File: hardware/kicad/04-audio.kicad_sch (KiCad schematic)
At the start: 9 parts, among them U5 PAM8403

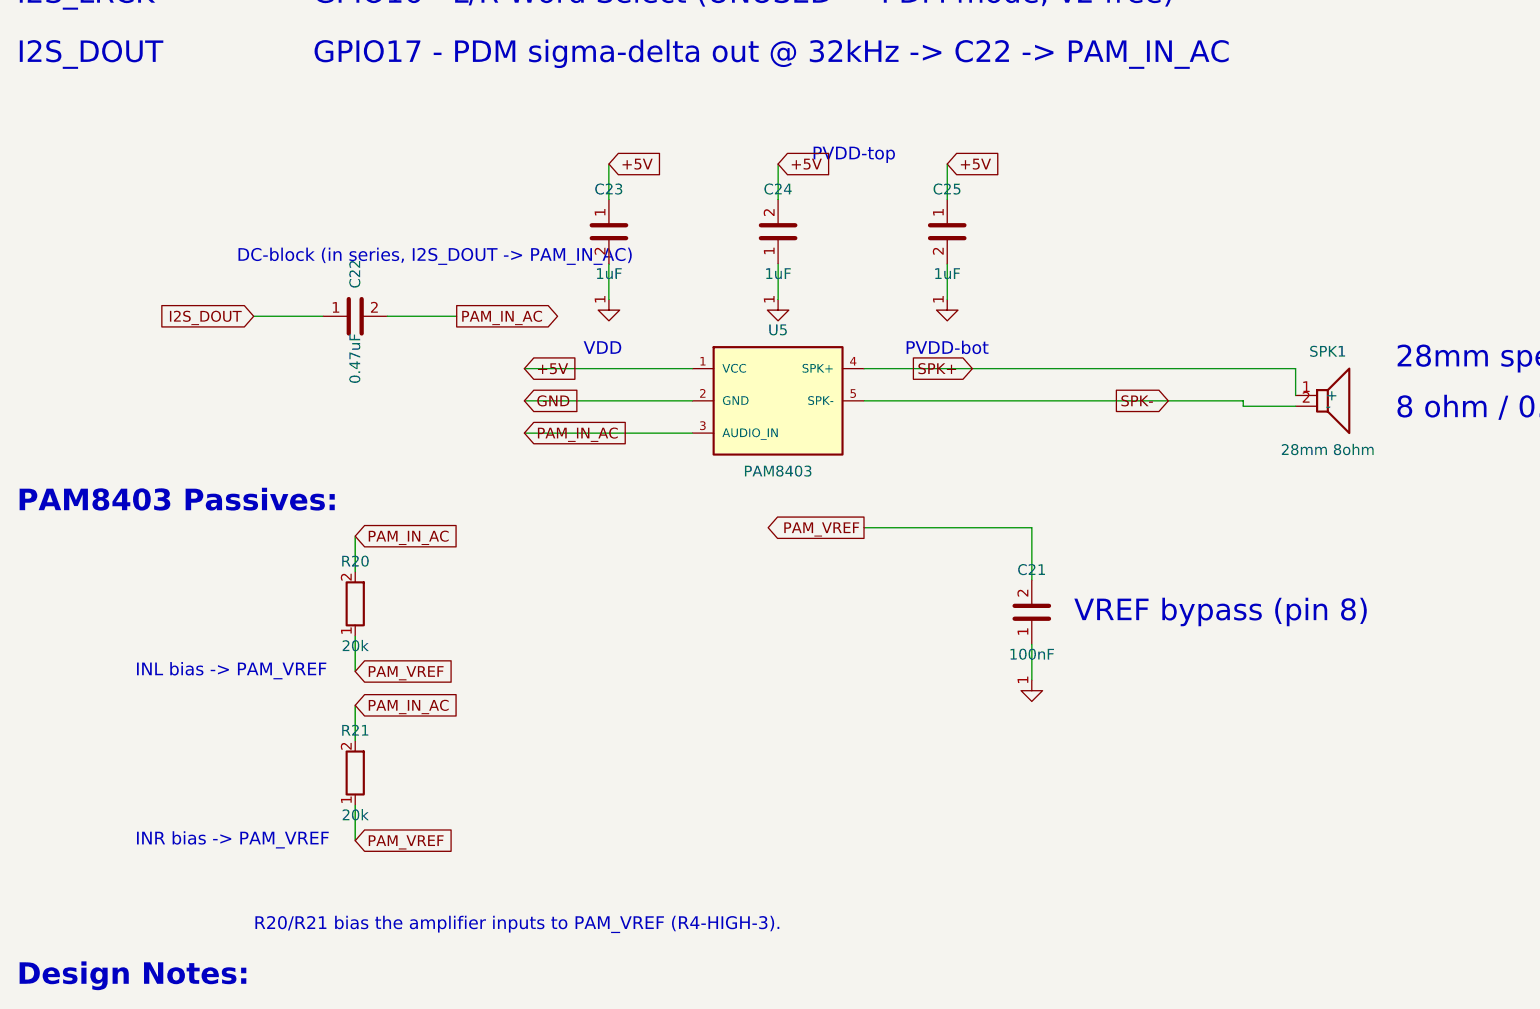
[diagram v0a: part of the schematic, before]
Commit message: feat(containment): layer 6 — ERC warning burn-down, 676 to ZERO, gate at all severities
Three root causes, three fixes in the schematic generator:

- 507 endpoint_off_grid: sheets lay out on a human 1 mm grid while KiCad
  connects on 1.27 mm. snap() in kicad_primitives now grid-snaps every
  connection-bearing coordinate at emission. Snapping is monotonic and
  distributes over the library's grid-multiple pin offsets, so points
  that coincided before still coincide after; zero-length stub wires
  that collapse onto their anchor are dropped.
- The stragglers came from three symbols whose pin connection points
  were themselves off-grid: BAT54C (±5.0 → ±5.08, top 5.0 → 5.08, used
  by D1 and Q1), USBLC6-2SC6 (±10.0 → ±10.16), Speaker (±0.635 →
  ±1.27). Their sheet wiring moved with them in the same commit.
- 169 lib_symbol_issues: bare lib_ids referenced library "" which no
  configuration includes. Symbols are now emu:<name>, resolved by a
  generated hardware/kicad/sym-lib-table + emu.kicad_sym built from the
  same SYMBOLS strings as the embedded caches — cache and library
  cannot disagree by construction.

verify_erc now runs --severity-all against a ZERO baseline: from zero,
any new warning is a regression a specific change introduced. The
website's per-sheet SVGs/PDFs are re-rendered, and the "Download all
sheets" PDF — a one-off hand merge nothing regenerated, stale since the
R25 respin — is now merged by render-schematics.sh from the exported
sheets.

Suite: 85/85 green; netlist_diff vs PCB confirms connectivity unchanged.

Co-Authored-By: Claude Fable 5 <noreply@anthropic.com>
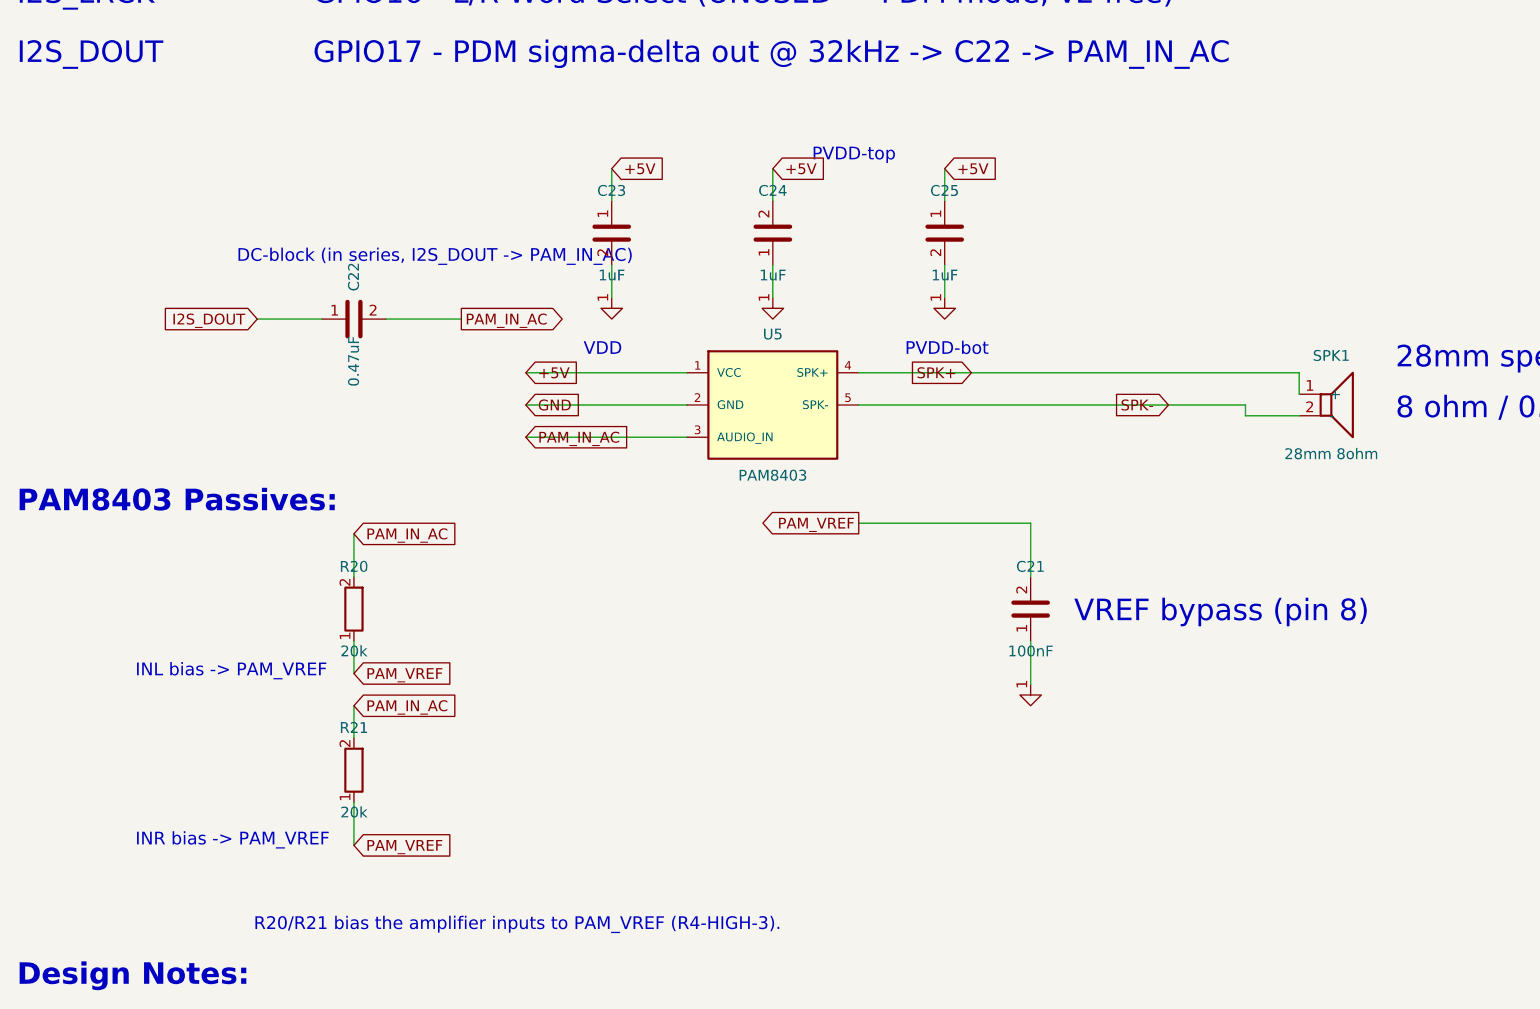
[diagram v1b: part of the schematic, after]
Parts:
- C21, C22, C23, C24, C25: symbol C -> emu:C
- R20, R21: symbol R -> emu:R
- SPK1: symbol Speaker -> emu:Speaker
- U5: symbol PAM8403_Module -> emu:PAM8403_Module
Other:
- moved on the sheet: C24, R20, SPK1, U5

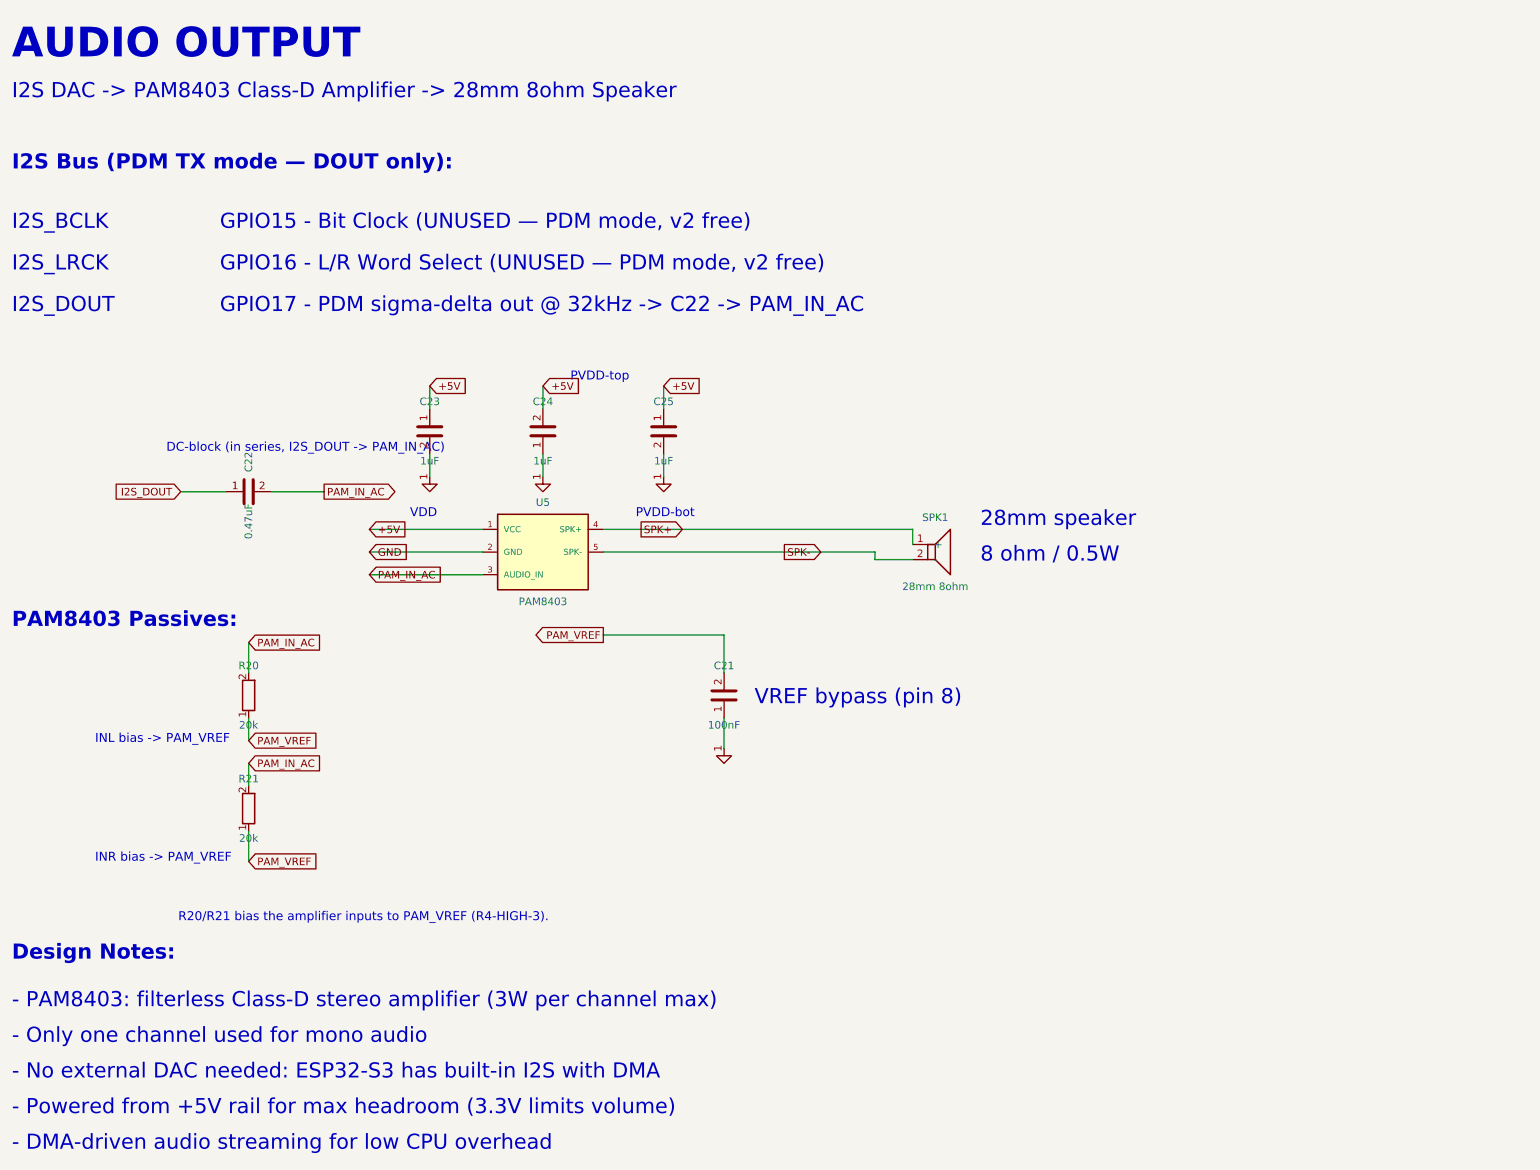
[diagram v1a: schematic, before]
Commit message: schematic: zero rendered text overlaps + real P-MOSFET artwork for Q1/Q2
The rendered sheets carried 75 text-on-text collisions the overlap gate
could not see: its model missed pin-number digits, KiCad's mirrored
field justification on 180-degree symbols, and global-label extents.
Root fixes in the generator:

- symbol() now places Reference/Value per part class: beside the body
  for two-pin verticals (R/C/L/Battery), stacked above for LEDs and the
  big ICs whose bottom pin numbers the old centred Value printed over,
  with per-call overrides where a zone is tight. On 180-rotated symbols
  the emitted justification is pre-mirrored, because KiCad flips it.
- Q1/Q2 get PMOS_SOT23 — same pin coordinates as the BAT54C symbol they
  were drawn with (wires and netlist untouched), but the artwork is now
  a P-MOSFET instead of a dual Schottky diode.
- Sheet-level relayouts: decoupling row on 02 spread to 11 mm pitch,
  menu-combo D1 zone on 06, FPC header on 03, PAM bias notes on 04,
  IP5306 KEY exit and the whole power-switch zone on 01.
- ESP32 module pin 41 name blanked — two "GND"s 2.54 mm apart printed
  into each other; number, type and net unchanged.

New gate: verify_schematic_render_overlaps.py exports each sheet to SVG
via kicad-cli and fails if any two DRAWN text runs intersect — ground
truth instead of a re-derived model (47 hits on the old sheet 01, 0
now). Wired into verify-all; dispatch mutation tests 14/14.

Netlist invariance: verify_netlist_diff 4/4, ERC clean at every
severity, schematic-PCB sync green. Website SVG/PDF re-rendered.

Co-Authored-By: Claude Fable 5 <noreply@anthropic.com>
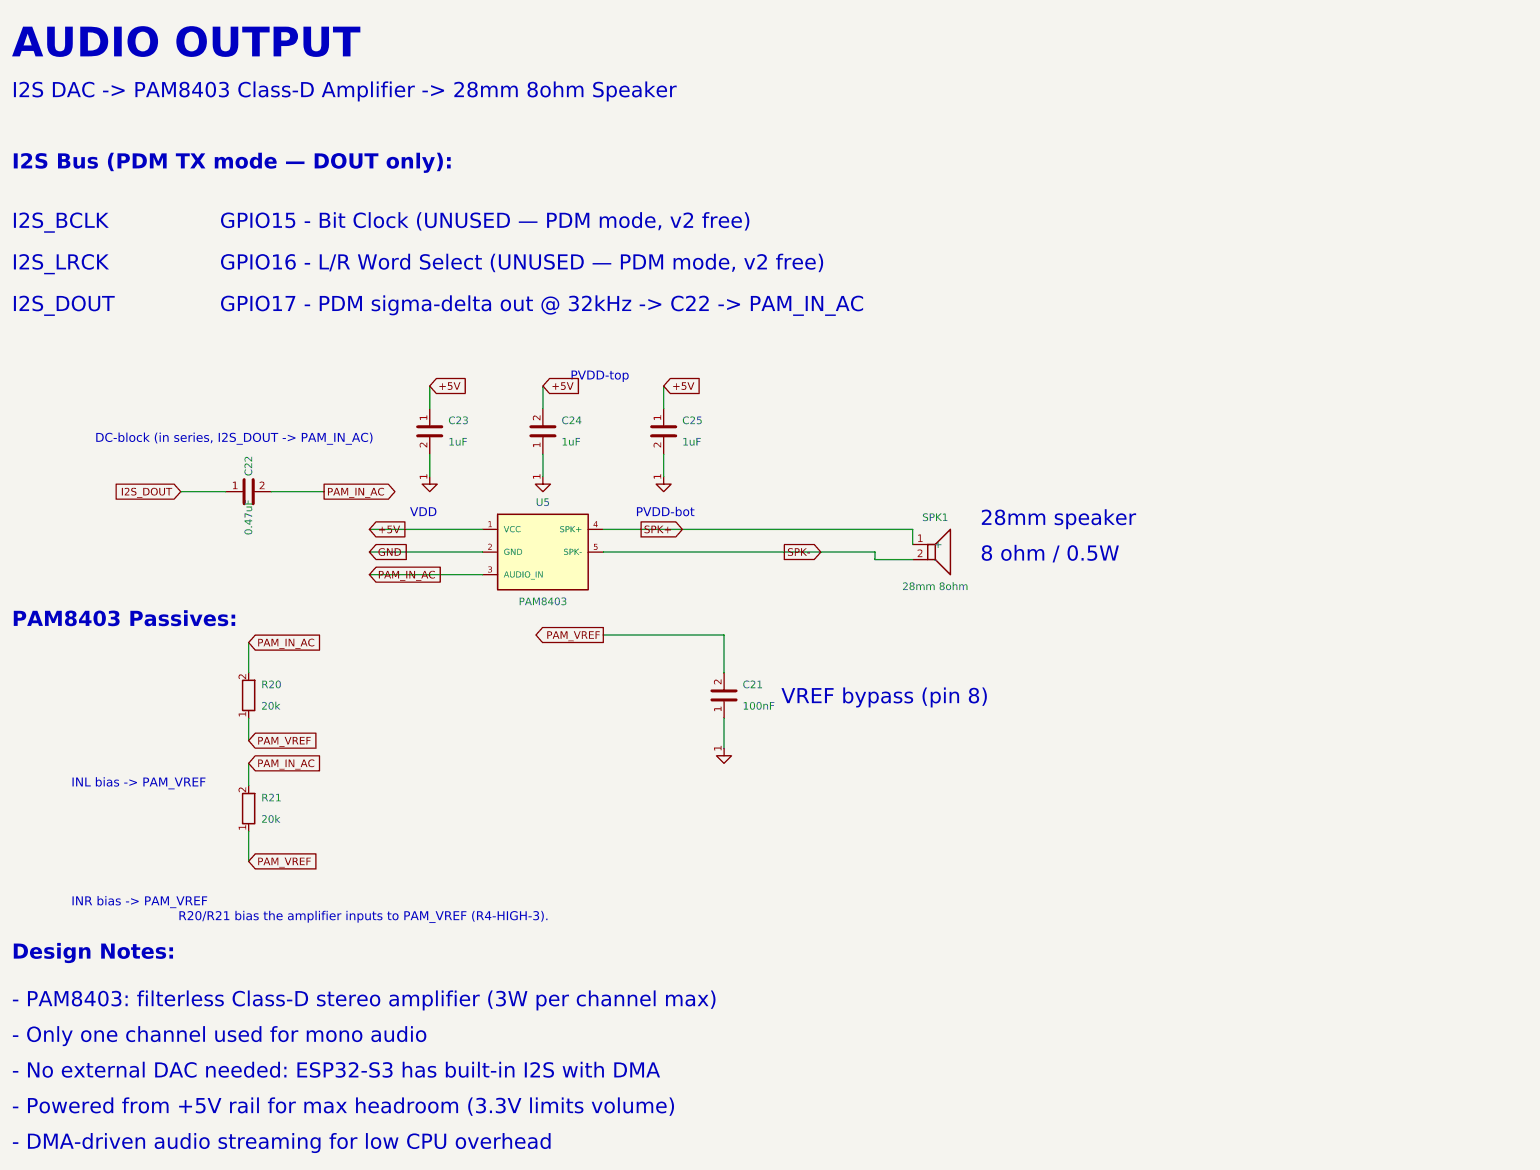
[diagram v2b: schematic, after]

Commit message: Add 3.5mm headphone jack (J5) with hardware speaker auto-mute
New audio output: HOOYA PJ-327A jack (LCSC C19712376) on the bottom
board edge at x=52, between the power switch and USB-C, fed by a
passive line-out tapped from I2S_DOUT UPSTREAM of the PAM8403 — its
filterless BTL outputs must never reach a ground-referenced jack.

Signal chain (sheet 04): I2S_DOUT -> R35 150R / R36 470R divider with
C34 47nF PDM low-pass (~30 kHz) -> C35 47uF AC coupling with R39 4.7k
DC bleed -> R37/R38 33R into tip and ring (mono to both channels).

Auto-mute, zero firmware: the jack tip's normally-closed rest contact
(pin 6, JACK_DET) parks Q3's (2N7002) gate at the tip's ~0V DC while
unplugged; inserting a plug opens the contact, R40 220k pulls the gate
to +3V3 and Q3's open drain pulls the PAM8403 MUTE pin (U5.5) low.
MUTE has an internal pull-up (Diodes datasheet), so the historic
VDD(6)->MUTE(5)->PVDD(4) +5V strap is removed and pin 5 now carries
PAM_MUTE; pins 4/6 keep their own +5V feeds.

Layout: the board's bottom half is fenced by the button-matrix B.Cu
verticals and the 11-row F.Cu bottom highway (inventory documented at
routing/_shared.py::J5_POS). The filter cluster lives in the empty
north pocket (x 44-52, y 17-41); R37/R38 in the P1 pocket; R40/Q3 in
P2a; PAM_MUTE crosses the board on F.Cu at y=22.5. BTN_RIGHT and BTN_Y
get local detours around J5's two NPTH locating holes.

Gates: verify-all 104/104 green. New nets classified in the net
explorer; polarity/datasheet/netlist-diff models updated to the new
MUTE topology; PJ-327A whitelisted where package families are
enumerated; Q3 added to the SOT-23-3 CPL rotation-law exceptions
(cpl=180 at KiCad 270, family arithmetic from Q1/Q2/D1). Enclosure
gets a 6.5mm jack opening next to the power switch cutout.

Order impact: this supersedes the v4.6.1 JLC set — regenerate/upload
and run the first-article check (J5 + Q3 orientation) before payment.

Co-Authored-By: Claude Fable 5 <noreply@anthropic.com>
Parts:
- added C34: 47nF, symbol emu:C
- added C35: 47uF, symbol emu:C
- added J5: PJ-327A, symbol emu:AudioJack_PJ327A
- added Q3: 2N7002, symbol emu:NMOS_SOT23
- added R35: 150R, symbol emu:R
- added R36: 470R, symbol emu:R
- added R37, R38: 33R, symbol emu:R
- added R39: 4.7k, symbol emu:R
- added R40: 220k, symbol emu:R
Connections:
- net GND: now also C34.2, J5.3 (SLV), Q3.2 (S), R36.2, R39.2
- net I2S_DOUT: now also R35.1
- new net +3V3: R40.1
- new net HP_AC: C35.2, R37.1, R38.1, R39.1
- new net HP_FILT: C34.1, C35.1, R35.2, R36.1
- new net HP_L: J5.2 (TIP), R37.2
- new net HP_R: J5.5 (RING), R38.2
- new net JACK_DET: J5.6 (TSW), Q3.1 (G), R40.2
- new net PAM_MUTE: Q3.3 (D), U5.6 (MUTE)
- no-connect marks 0 -> 1
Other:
- note added: "(audio peaks < 2N7002 Vgs(th) min - no chatter)."
- note added: "HEADPHONE OUT + AUTO-MUTE"
- note added: "Passive line-out from PDM (pre-amplifier tap)"
- note added: "Plug inserted -> TSW opens -> R40 pulls JACK_DET"
- note added: "Unplugged: TSW ties the gate to the tip's ~0V DC"
- note added: "high -> Q3 pulls PAM8403 MUTE low (speaker off)."
- title: Audio - I2S -> PAM8403 -> Speaker -> Audio - I2S -> PAM8403 -> Speaker + Headphone Jack
